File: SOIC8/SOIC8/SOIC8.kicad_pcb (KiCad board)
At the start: 2 copper layers, 10.7 x 10.7 mm, 7 parts, among them J1 Conn_01x04, J2 Conn_01x04

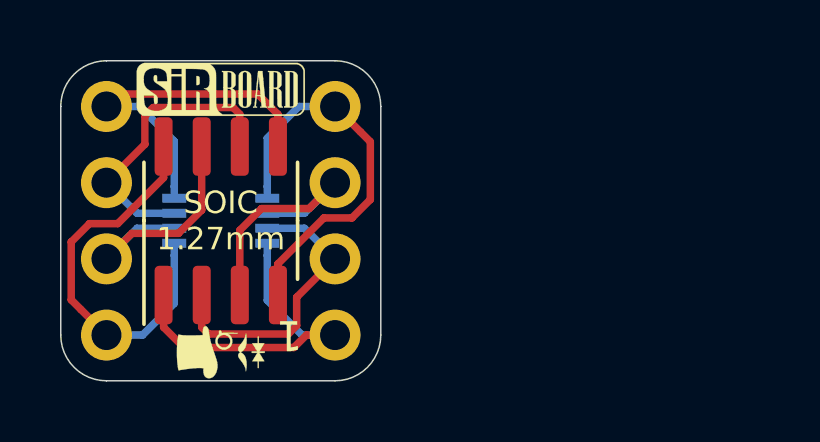
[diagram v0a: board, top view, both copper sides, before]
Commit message: SOIC20 and SOIC28 Added
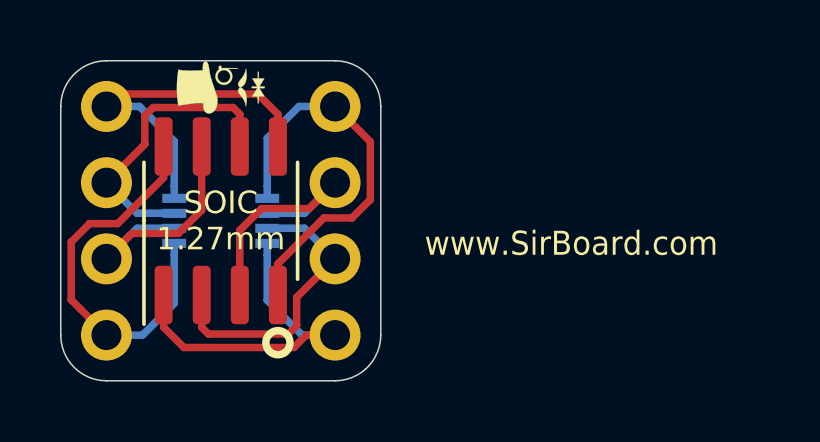
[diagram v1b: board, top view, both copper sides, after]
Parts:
- G***: moved to B.Cu
- moved G*** 8.83 mm to (179.1, 71.5)
- moved G*** 7.30 mm to (179.1, 78.9)
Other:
- board text added: "www.SirBoard.com"
- board text removed: "1"

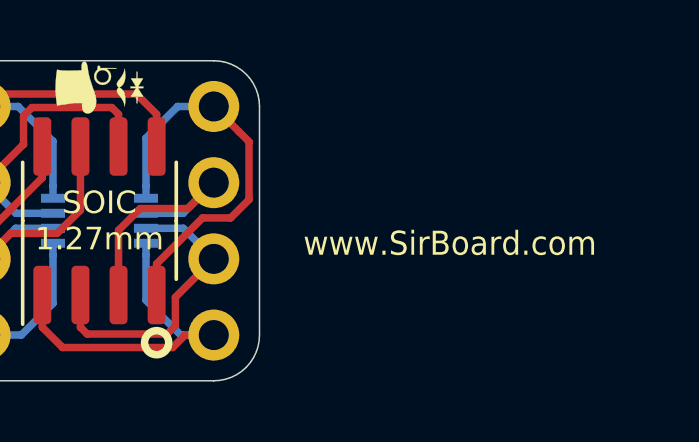
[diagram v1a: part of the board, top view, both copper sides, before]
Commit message: Silkscreens and sizes updated
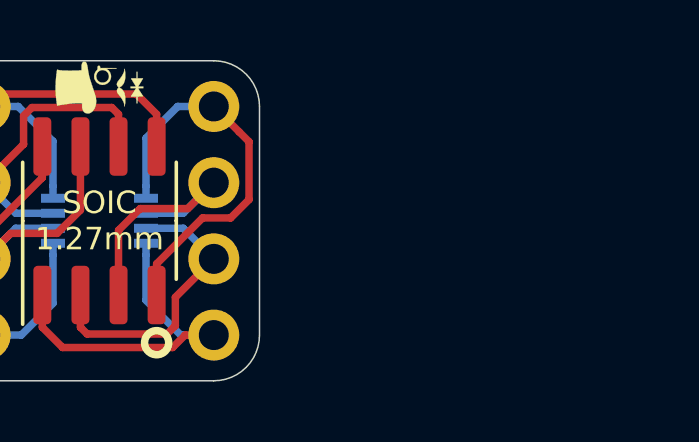
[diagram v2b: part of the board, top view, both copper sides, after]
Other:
- board text removed: "1 2 3 4"
- board text removed: "8 7 6 5"
- board text removed: "www.SirBoard.com"
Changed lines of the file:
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@@
   (general
     (thickness 1.6)
-    (drawings 15)
+    (drawings 14)
     (tracks 67)
     (zones 0)
@@
   (layers
     (0 F.Cu signal)
-    (31 B.Cu signal hide)
+    (31 B.Cu signal)
     (32 B.Adhes user hide)
     (33 F.Adhes user hide)
     (34 B.Paste user hide)
     (35 F.Paste user hide)
-    (36 B.SilkS user hide)
+    (36 B.SilkS user)
     (37 F.SilkS user)
     (38 B.Mask user hide)
     (39 F.Mask user hide)
-    (40 Dwgs.User user hide)
+    (40 Dwgs.User user)
     (41 Cmts.User user hide)
     (42 Eco1.User user hide)
@@
     )
   )
+  (dimension 10.668 (width 0.15) (layer Dwgs.User)
+    (gr_text "10.668 mm" (at 191.292 75.946 270) (layer Dwgs.User)
+      (effects (font (size 1 1) (thickness 0.15)))
+    )
+    (feature1 (pts (xy 184.404 81.28) (xy 190.578421 81.28)))
+    (feature2 (pts (xy 184.404 70.612) (xy 190.578421 70.612)))
+    (crossbar (pts (xy 189.992 70.612) (xy 189.992 81.28)))
+    (arrow1a (pts (xy 189.992 81.28) (xy 189.405579 80.153496)))
+    (arrow1b (pts (xy 189.992 81.28) (xy 190.578421 80.153496)))
+    (arrow2a (pts (xy 189.992 70.612) (xy 189.405579 71.738504)))
+    (arrow2b (pts (xy 189.992 70.612) (xy 190.578421 71.738504)))
+  )
+  (dimension 10.668 (width 0.15) (layer Dwgs.User)
+    (gr_text "10.668 mm" (at 179.07 66.264) (layer Dwgs.User)
+      (effects (font (size 1 1) (thickness 0.15)))
+    )
+    (feature1 (pts (xy 184.404 70.612) (xy 184.404 66.977579)))
+    (feature2 (pts (xy 173.736 70.612) (xy 173.736 66.977579)))
+    (crossbar (pts (xy 173.736 67.564) (xy 184.404 67.564)))
+    (arrow1a (pts (xy 184.404 67.564) (xy 183.277496 68.150421)))
+    (arrow1b (pts (xy 184.404 67.564) (xy 183.277496 66.977579)))
+    (arrow2a (pts (xy 173.736 67.564) (xy 174.862504 68.150421)))
+    (arrow2b (pts (xy 173.736 67.564) (xy 174.862504 66.977579)))
+  )
+  (gr_circle (center 176.784 80.518) (end 177.185609 80.518) (layer B.SilkS) (width 0.25))
   (gr_circle (center 180.975 80.01) (end 181.376609 80.01) (layer F.SilkS) (width 0.25))
-  (gr_circle (center 176.784 80.645) (end 177.185609 80.645) (layer B.SilkS) (width 0.25))
-  (gr_text www.SirBoard.com (at 190.754 76.708) (layer F.SilkS)
-    (effects (font (size 0.8 0.75) (thickness 0.1)))
-  )
   (gr_text "VSSOP\n0.5mm" (at 179.07 76.073 90) (layer B.SilkS)
     (effects (font (size 0.75 0.75) (thickness 0.15)) (justify mirror))
@@
   (gr_arc (start 175.26 72.136) (end 175.26 70.612) (angle -90) (layer Edge.Cuts) (width 0.05))
   (gr_arc (start 182.88 72.136) (end 184.404 72.136) (angle -90) (layer Edge.Cuts) (width 0.05))
-  (gr_text "8\n\n7\n\n6\n\n5" (at 164.7444 99.5934 180) (layer B.SilkS)
-    (effects (font (size 0.75 0.75) (thickness 0.15)) (justify mirror))
-  )
-  (gr_text "1\n\n2\n\n3\n\n4" (at 162.3314 99.7966 180) (layer B.SilkS)
-    (effects (font (size 0.75 0.75) (thickness 0.15)) (justify mirror))
-  )
   (segment (start 180.975 72.396) (end 180.975 73.371) (width 0.25) (layer F.Cu) (net 1))
   (segment (start 180.29998 71.72098) (end 180.975 72.396) (width 0.25) (layer F.Cu) (net 1))

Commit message: Pin Numbering edited
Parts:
- J1, J2: moved to B.Cu
- turned G*** to 90 degrees
- turned J1 to 0 degrees
- turned J2 to 0 degrees
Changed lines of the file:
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@@
   )
   (module logo:logo47x67 (layer B.Cu)
-    (at 179.07 72.5805 270)
+    (at 179.07 72.5805 90)
     (fp_text reference G*** (at 0 0 270) (layer B.SilkS) hide
       (effects (font (size 1.524 1.524) (thickness 0.3)) (justify mirror))
@@
       (xy -0.0381 -1.68275) (xy 0.04445 -1.68275) (xy 0.04445 -1.829329)) (layer B.SilkS) (width 0.01))
   )
-  (module Connector_PinHeader_2.54mm:PinHeader_1x04_P2.54mm_Vertical (layer F.Cu)
-    (at 175.26 79.756 180)
+  (module Connector_PinHeader_2.54mm:PinHeader_1x04_P2.54mm_Vertical (layer B.Cu)
+    (at 175.26 79.756)
     (descr "Through hole straight pin header, 1x04, 2.54mm pitch, single row")
     (tags "Through hole pin header THT 1x04 2.54mm single row")
-    (fp_text reference J1 (at 0 -2.33 180) (layer F.SilkS) hide
-      (effects (font (size 1 1) (thickness 0.15)))
-    )
-    (fp_text value Conn_01x04 (at 0 9.95 180) (layer F.Fab)
-      (effects (font (size 1 1) (thickness 0.15)))
-    )
-    (fp_line (start -0.635 -1.27) (end 1.27 -1.27) (layer F.Fab) (width 0.1))
-    (fp_line (start 1.27 -1.27) (end 1.27 8.89) (layer F.Fab) (width 0.1))
-    (fp_line (start 1.27 8.89) (end -1.27 8.89) (layer F.Fab) (width 0.1))
-    (fp_line (start -1.27 8.89) (end -1.27 -0.635) (layer F.Fab) (width 0.1))
-    (fp_line (start -1.27 -0.635) (end -0.635 -1.27) (layer F.Fab) (width 0.1))
-    (fp_line (start -1.8 -1.8) (end -1.8 9.4) (layer F.CrtYd) (width 0.05))
-    (fp_line (start -1.8 9.4) (end 1.8 9.4) (layer F.CrtYd) (width 0.05))
-    (fp_line (start 1.8 9.4) (end 1.8 -1.8) (layer F.CrtYd) (width 0.05))
-    (fp_line (start 1.8 -1.8) (end -1.8 -1.8) (layer F.CrtYd) (width 0.05))
-    (fp_text user %R (at 0 3.81 270) (layer F.Fab)
-      (effects (font (size 1 1) (thickness 0.15)))
-    )
-    (pad 1 thru_hole circle (at 0 0 180) (size 1.7 1.7) (drill 1) (layers *.Cu *.Mask)
+    (fp_text reference J1 (at 0 2.33 180) (layer B.SilkS) hide
+      (effects (font (size 1 1) (thickness 0.15)) (justify mirror))
+    )
+    (fp_text value Conn_01x04 (at 0 -9.95 180) (layer B.Fab)
+      (effects (font (size 1 1) (thickness 0.15)) (justify mirror))
+    )
+    (fp_line (start -0.635 1.27) (end 1.27 1.27) (layer B.Fab) (width 0.1))
+    (fp_line (start 1.27 1.27) (end 1.27 -8.89) (layer B.Fab) (width 0.1))
+    (fp_line (start 1.27 -8.89) (end -1.27 -8.89) (layer B.Fab) (width 0.1))
+    (fp_line (start -1.27 -8.89) (end -1.27 0.635) (layer B.Fab) (width 0.1))
+    (fp_line (start -1.27 0.635) (end -0.635 1.27) (layer B.Fab) (width 0.1))
+    (fp_line (start -1.8 1.8) (end -1.8 -9.4) (layer B.CrtYd) (width 0.05))
+    (fp_line (start -1.8 -9.4) (end 1.8 -9.4) (layer B.CrtYd) (width 0.05))
+    (fp_line (start 1.8 -9.4) (end 1.8 1.8) (layer B.CrtYd) (width 0.05))
+    (fp_line (start 1.8 1.8) (end -1.8 1.8) (layer B.CrtYd) (width 0.05))
+    (fp_text user %R (at 0 -3.81 90) (layer B.Fab)
+      (effects (font (size 1 1) (thickness 0.15)) (justify mirror))
+    )
+    (pad 1 thru_hole circle (at 0 0) (size 1.7 1.7) (drill 1) (layers *.Cu *.Mask)
       (net 4 "Net-(J1-Pad1)"))
-    (pad 2 thru_hole oval (at 0 2.54 180) (size 1.7 1.7) (drill 1) (layers *.Cu *.Mask)
+    (pad 2 thru_hole oval (at 0 -2.54) (size 1.7 1.7) (drill 1) (layers *.Cu *.Mask)
       (net 3 "Net-(J1-Pad2)"))
-    (pad 3 thru_hole oval (at 0 5.08 180) (size 1.7 1.7) (drill 1) (layers *.Cu *.Mask)
+    (pad 3 thru_hole oval (at 0 -5.08) (size 1.7 1.7) (drill 1) (layers *.Cu *.Mask)
       (net 2 "Net-(J1-Pad3)"))
-    (pad 4 thru_hole oval (at 0 7.62 180) (size 1.7 1.7) (drill 1) (layers *.Cu *.Mask)
+    (pad 4 thru_hole oval (at 0 -7.62) (size 1.7 1.7) (drill 1) (layers *.Cu *.Mask)
       (net 1 "Net-(J1-Pad4)"))
     (model ${KISYS3DMOD}/Connector_PinHeader_2.54mm.3dshapes/PinHeader_1x04_P2.54mm_Vertical.wrl
@@
     )
   )
-  (module Connector_PinHeader_2.54mm:PinHeader_1x04_P2.54mm_Vertical (layer F.Cu)
-    (at 182.88 79.756 180)
+  (module Connector_PinHeader_2.54mm:PinHeader_1x04_P2.54mm_Vertical (layer B.Cu)
+    (at 182.88 79.756)
     (descr "Through hole straight pin header, 1x04, 2.54mm pitch, single row")
     (tags "Through hole pin header THT 1x04 2.54mm single row")
-    (fp_text reference J2 (at 0 -2.33 180) (layer F.SilkS) hide
-      (effects (font (size 1 1) (thickness 0.15)))
-    )
-    (fp_text value Conn_01x04 (at 0 9.95 180) (layer F.Fab)
-      (effects (font (size 1 1) (thickness 0.15)))
-    )
-    (fp_line (start -0.635 -1.27) (end 1.27 -1.27) (layer F.Fab) (width 0.1))
-    (fp_line (start 1.27 -1.27) (end 1.27 8.89) (layer F.Fab) (width 0.1))
-    (fp_line (start 1.27 8.89) (end -1.27 8.89) (layer F.Fab) (width 0.1))
-    (fp_line (start -1.27 8.89) (end -1.27 -0.635) (layer F.Fab) (width 0.1))
-    (fp_line (start -1.27 -0.635) (end -0.635 -1.27) (layer F.Fab) (width 0.1))
-    (fp_line (start -1.8 -1.8) (end -1.8 9.4) (layer F.CrtYd) (width 0.05))
-    (fp_line (start -1.8 9.4) (end 1.8 9.4) (layer F.CrtYd) (width 0.05))
-    (fp_line (start 1.8 9.4) (end 1.8 -1.8) (layer F.CrtYd) (width 0.05))
-    (fp_line (start 1.8 -1.8) (end -1.8 -1.8) (layer F.CrtYd) (width 0.05))
-    (fp_text user %R (at 0 3.81 270) (layer F.Fab)
-      (effects (font (size 1 1) (thickness 0.15)))
-    )
-    (pad 1 thru_hole circle (at 0 0 180) (size 1.7 1.7) (drill 1) (layers *.Cu *.Mask)
+    (fp_text reference J2 (at 0 2.33 180) (layer B.SilkS) hide
+      (effects (font (size 1 1) (thickness 0.15)) (justify mirror))
+    )
+    (fp_text value Conn_01x04 (at 0 -9.95 180) (layer B.Fab)
+      (effects (font (size 1 1) (thickness 0.15)) (justify mirror))
+    )
+    (fp_line (start -0.635 1.27) (end 1.27 1.27) (layer B.Fab) (width 0.1))
+    (fp_line (start 1.27 1.27) (end 1.27 -8.89) (layer B.Fab) (width 0.1))
+    (fp_line (start 1.27 -8.89) (end -1.27 -8.89) (layer B.Fab) (width 0.1))
+    (fp_line (start -1.27 -8.89) (end -1.27 0.635) (layer B.Fab) (width 0.1))
+    (fp_line (start -1.27 0.635) (end -0.635 1.27) (layer B.Fab) (width 0.1))
+    (fp_line (start -1.8 1.8) (end -1.8 -9.4) (layer B.CrtYd) (width 0.05))
+    (fp_line (start -1.8 -9.4) (end 1.8 -9.4) (layer B.CrtYd) (width 0.05))
+    (fp_line (start 1.8 -9.4) (end 1.8 1.8) (layer B.CrtYd) (width 0.05))
+    (fp_line (start 1.8 1.8) (end -1.8 1.8) (layer B.CrtYd) (width 0.05))
+    (fp_text user %R (at 0 -3.81 90) (layer B.Fab)
+      (effects (font (size 1 1) (thickness 0.15)) (justify mirror))
+    )
+    (pad 1 thru_hole circle (at 0 0) (size 1.7 1.7) (drill 1) (layers *.Cu *.Mask)
       (net 8 "Net-(J2-Pad1)"))
-    (pad 2 thru_hole oval (at 0 2.54 180) (size 1.7 1.7) (drill 1) (layers *.Cu *.Mask)
+    (pad 2 thru_hole oval (at 0 -2.54) (size 1.7 1.7) (drill 1) (layers *.Cu *.Mask)
       (net 7 "Net-(J2-Pad2)"))
-    (pad 3 thru_hole oval (at 0 5.08 180) (size 1.7 1.7) (drill 1) (layers *.Cu *.Mask)
+    (pad 3 thru_hole oval (at 0 -5.08) (size 1.7 1.7) (drill 1) (layers *.Cu *.Mask)
       (net 6 "Net-(J2-Pad3)"))
-    (pad 4 thru_hole oval (at 0 7.62 180) (size 1.7 1.7) (drill 1) (layers *.Cu *.Mask)
+    (pad 4 thru_hole oval (at 0 -7.62) (size 1.7 1.7) (drill 1) (layers *.Cu *.Mask)
       (net 5 "Net-(J2-Pad4)"))
     (model ${KISYS3DMOD}/Connector_PinHeader_2.54mm.3dshapes/PinHeader_1x04_P2.54mm_Vertical.wrl
@@
   (gr_circle (center 176.784 80.518) (end 177.185609 80.518) (layer B.SilkS) (width 0.25))
   (gr_circle (center 180.975 80.01) (end 181.376609 80.01) (layer F.SilkS) (width 0.25))
-  (gr_text "VSSOP\n0.5mm" (at 179.07 76.073 90) (layer B.SilkS)
+  (gr_text "VSSOP\n0.5mm" (at 179.07 76.073 270) (layer B.SilkS)
     (effects (font (size 0.75 0.75) (thickness 0.15)) (justify mirror))
   )

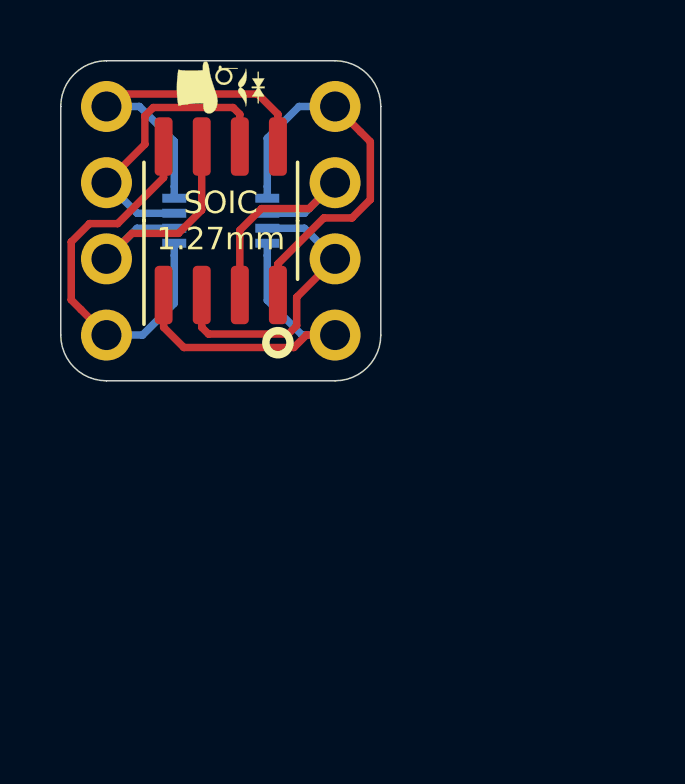
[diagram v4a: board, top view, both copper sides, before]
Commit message: Numbering Orientation Edited
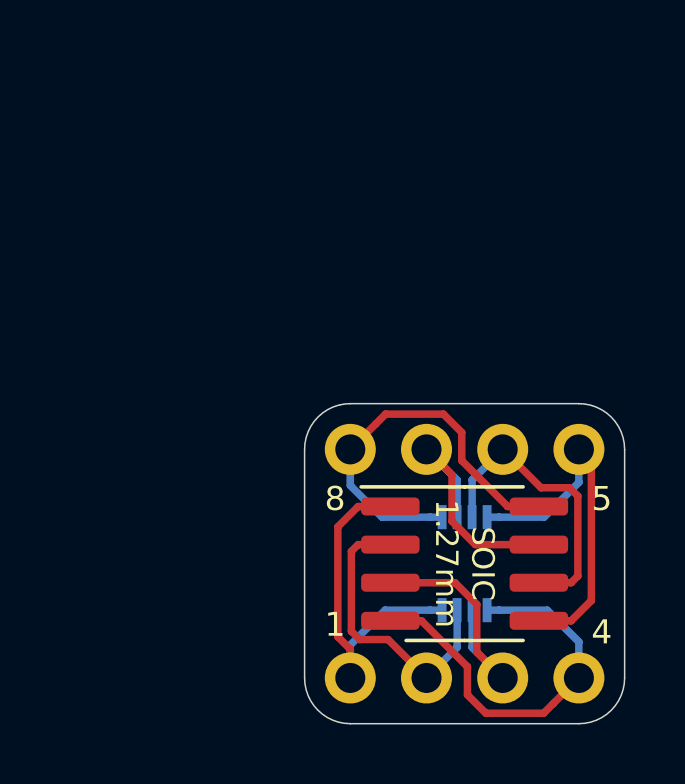
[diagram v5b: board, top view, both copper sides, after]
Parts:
- removed the G*** at (179.1, 71.5)
- removed the G*** at (179.1, 72.6)
- J1, J2: moved to F.Cu
- moved REF** 14.0 mm to (187.2, 87.4), turned to 270 degrees
- moved SOIC/SOIJ 14.0 mm to (187.2, 87.4), turned to 0 degrees
- moved J2 11.4 mm to (183.4, 91.2), turned to 90 degrees
- moved G*** 9.98 mm to (184.3, 87.4), turned to 270 degrees
- moved J1 8.98 mm to (183.4, 83.6), turned to 90 degrees
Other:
- board text added: "1"
- board text added: "4"
- board text added: "5"
- board text added: "8"
